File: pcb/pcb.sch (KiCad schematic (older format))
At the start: 0 parts

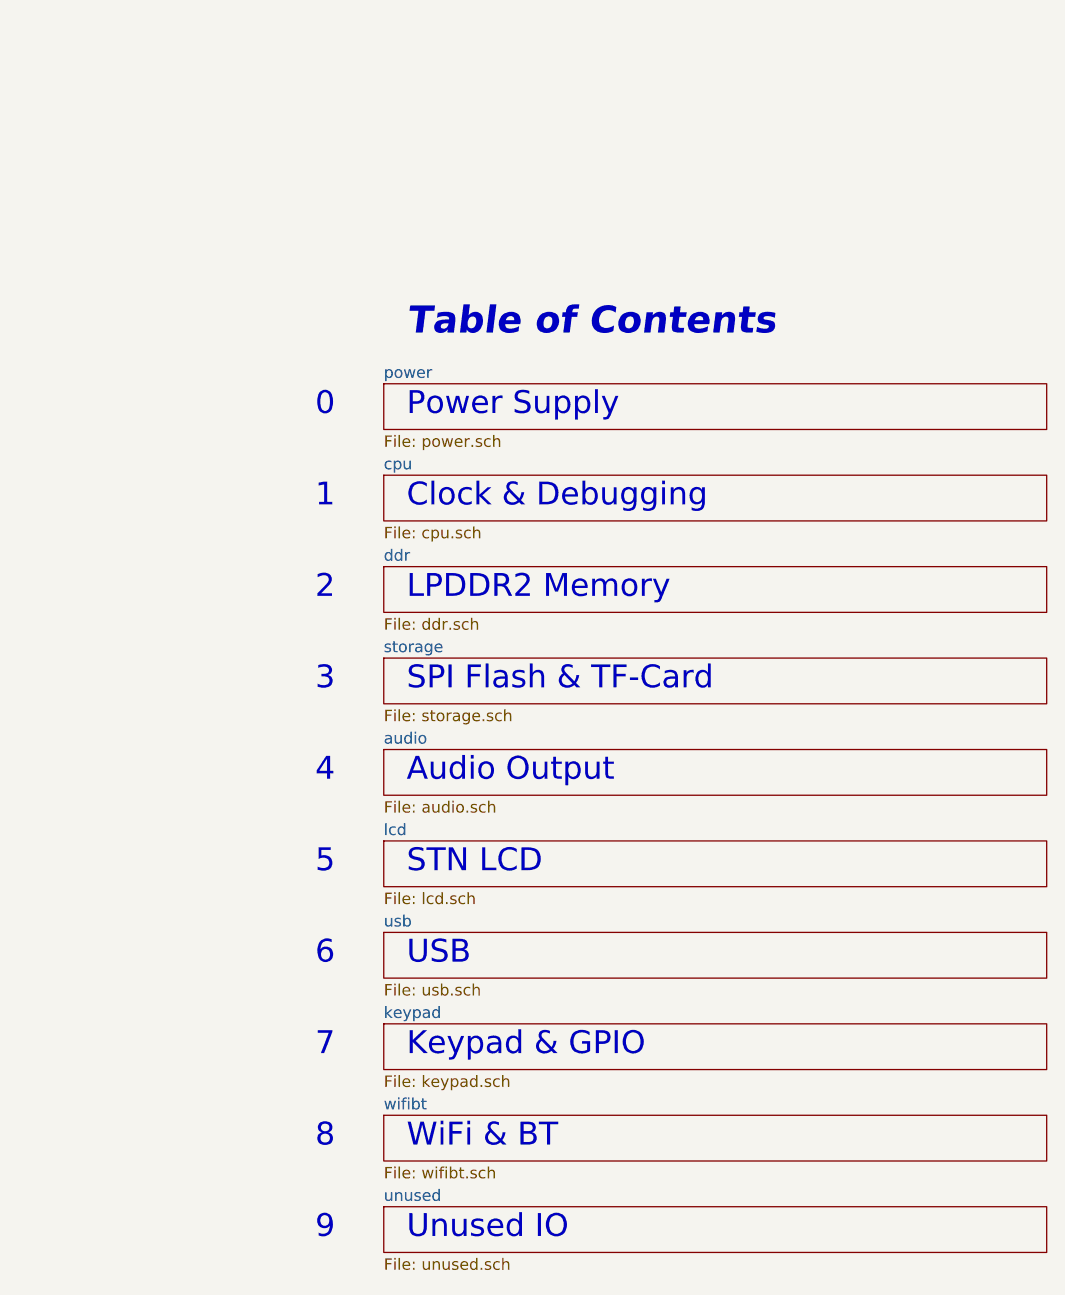
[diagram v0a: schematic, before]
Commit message: pcb: adding lpc5500
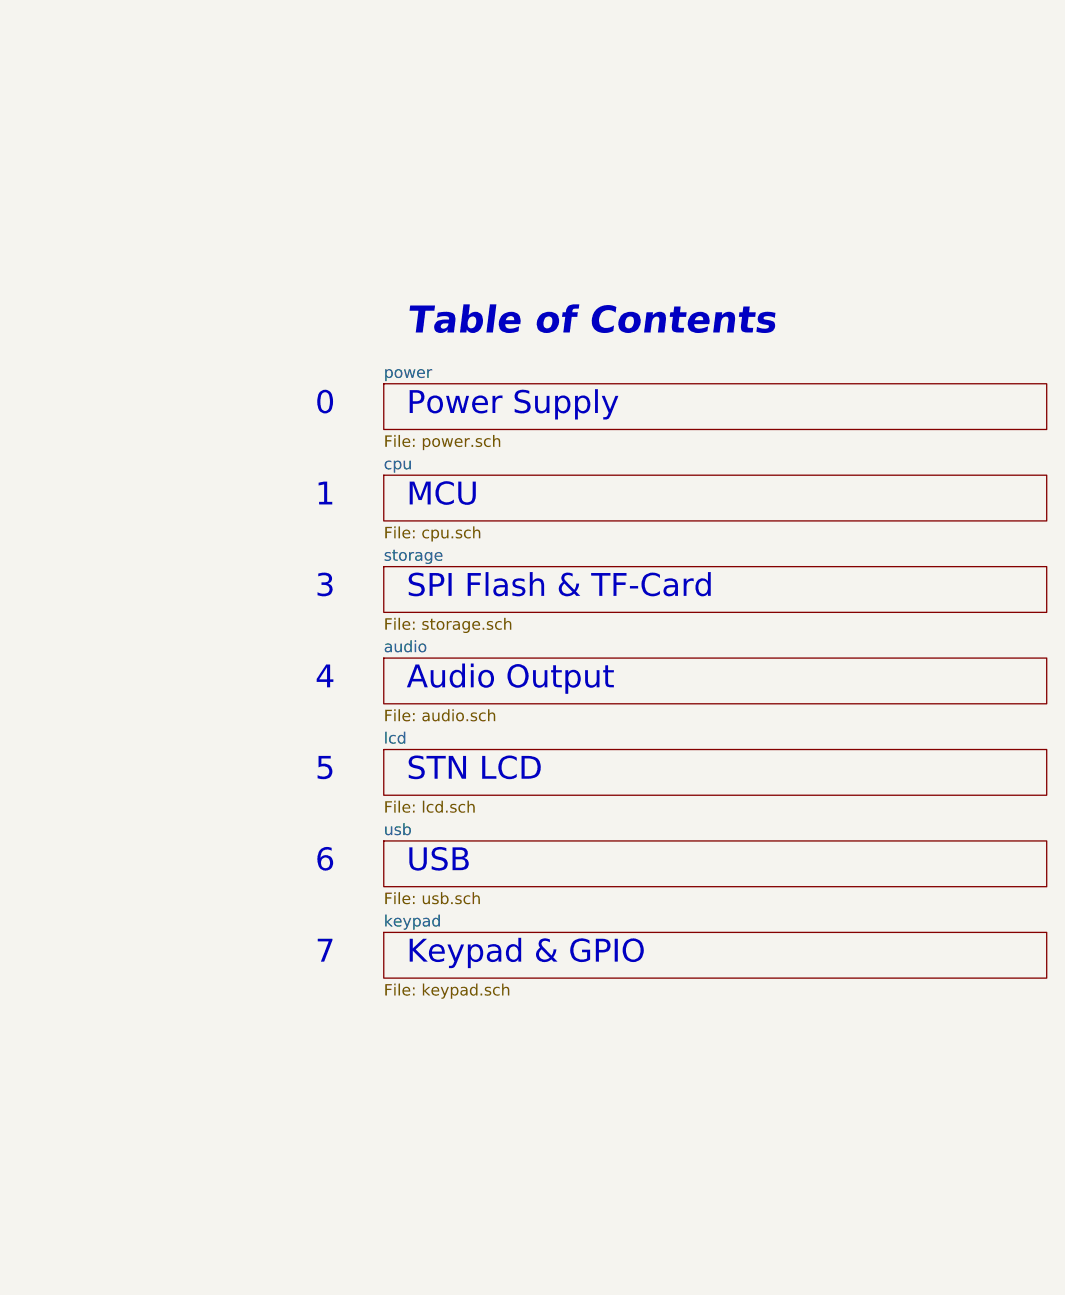
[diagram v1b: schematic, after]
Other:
- note added: "MCU"
- note removed: "2"
- note removed: "8"
- note removed: "9"
- note removed: "Clock & Debugging"
- note removed: "LPDDR2 Memory"
- note removed: "Unused IO"
- note removed: "WiFi & BT"
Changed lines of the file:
@@
 $Descr A4 11693 8268
 encoding utf-8
-Sheet 1 11
-Title "RhythmPocket"
-Date "2019-08-12"
-Rev "R0.2"
+Sheet 1 8
+Title "RhythmPocketLite"
+Date "2019-09-06"
+Rev "R0.1"
 Comp "ZephRay"
 Comment1 "zephray@outlook.com"
@@
 $Sheet
 S 1600 2400 2900 200
-U 5D5090CA
-F0 "ddr" 50
-F1 "ddr.sch" 50
-$EndSheet
-$Sheet
-S 1600 2800 2900 200
 U 5DB2122B
 F0 "storage" 50
@@
 $EndSheet
 $Sheet
-S 1600 3600 2900 200
+S 1600 3200 2900 200
 U 5DB51F59
 F0 "lcd" 50
@@
 $EndSheet
 Text Notes 1700 2150 0    100  ~ 0
-Clock & Debugging
+MCU
+Text Notes 1700 3350 0    100  ~ 0
+STN LCD
 Text Notes 1700 2550 0    100  ~ 0
-LPDDR2 Memory
-Text Notes 1700 3750 0    100  ~ 0
-STN LCD
-Text Notes 1700 2950 0    100  ~ 0
 SPI Flash & TF-Card
 Text Notes 1700 1400 0    118  Italic 24
@@
 Power Supply
 $Sheet
-S 1600 3200 2900 200
+S 1600 2800 2900 200
 U 5D438133
 F0 "audio" 50
 F1 "audio.sch" 50
 $EndSheet
-Text Notes 1700 3350 0    100  ~ 0
+Text Notes 1700 2950 0    100  ~ 0
 Audio Output\n
 $Sheet
-S 1600 4400 2900 200
+S 1600 4000 2900 200
 U 5D438406
 F0 "keypad" 50
 F1 "keypad.sch" 50
 $EndSheet
+Text Notes 1700 4150 0    100  ~ 0
+Keypad & GPIO
 $Sheet
-S 1600 5200 2900 200
-U 5D438456
-F0 "unused" 50
-F1 "unused.sch" 50
-$EndSheet
-Text Notes 1700 4550 0    100  ~ 0
-Keypad & GPIO
-Text Notes 1700 5350 0    100  ~ 0
-Unused IO
-$Sheet
-S 1600 4000 2900 200
+S 1600 3600 2900 200
 U 5D1A413B
 F0 "usb" 50
 F1 "usb.sch" 50
 $EndSheet
-Text Notes 1700 4150 0    100  ~ 0
+Text Notes 1700 3750 0    100  ~ 0
 USB
 Text Notes 1300 2150 0    100  ~ 0
 1
 Text Notes 1300 2550 0    100  ~ 0
-2
+3
 Text Notes 1300 2950 0    100  ~ 0
-3
+4
 Text Notes 1300 3350 0    100  ~ 0
-4
+5
 Text Notes 1300 3750 0    100  ~ 0
-5
+6
 Text Notes 1300 4150 0    100  ~ 0
-6
-Text Notes 1300 4550 0    100  ~ 0
 7
 Text Notes 1300 1750 0    100  ~ 0
 0
-Text Notes 1300 5350 0    100  ~ 0
-9
-$Sheet
-S 1600 4800 2900 200
-U 5D1BA41C
-F0 "wifibt" 50
-F1 "wifibt.sch" 50
-$EndSheet
-Text Notes 1300 4950 0    100  ~ 0
-8
-Text Notes 1700 4950 0    100  ~ 0
-WiFi & BT
 $EndSCHEMATC

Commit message: pcb: rev 0.1
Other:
- note added: "TF-Card"
- note removed: "SPI Flash & TF-Card"
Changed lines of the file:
@@
 STN LCD
 Text Notes 1700 2550 0    100  ~ 0
-SPI Flash & TF-Card
+TF-Card
 Text Notes 1700 1400 0    118  Italic 24
 Table of Contents

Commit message: pcb: use crystal instead
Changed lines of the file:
@@
 Text Notes 1300 1750 0    100  ~ 0
 0
+Entry Wire Line
+	0    0    100  100
 $EndSCHEMATC
